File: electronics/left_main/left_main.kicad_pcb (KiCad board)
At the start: 4 copper layers, 45 x 51 mm, 189 parts, among them IC1 AS3435-EQFM, IC2 AS3435-EQFM, J1 connectors_board, J10 right_side, J11 right_side, J12 right_side, J13 right_side, J14 right_side, J15 right_side, J16 right_side, J17 right_side, J18 right_side, J19 ear_sensor, J20 ear_sensor, J21 ear_sensor, J22 ear_sensor, J3 FF_MIC_L_+, J4 FF_MIC_L_-, J5 FB_MIC_L_+, J6 FB_MIC_L_-, J7 HP_L_+, J8 HP_L_-, J9 right_side, SW2 reset_button, U1 BM83, U2 ATSAMD21G18_QFN, U3 MCP73831T-2ACI/OT, U4 SPX3819-3.3, U5 MAX17048G+T10, U6 AP2127K-1.8, U7 AP22814AW5, U8 AP22814AW5, Y1 32.768KHz

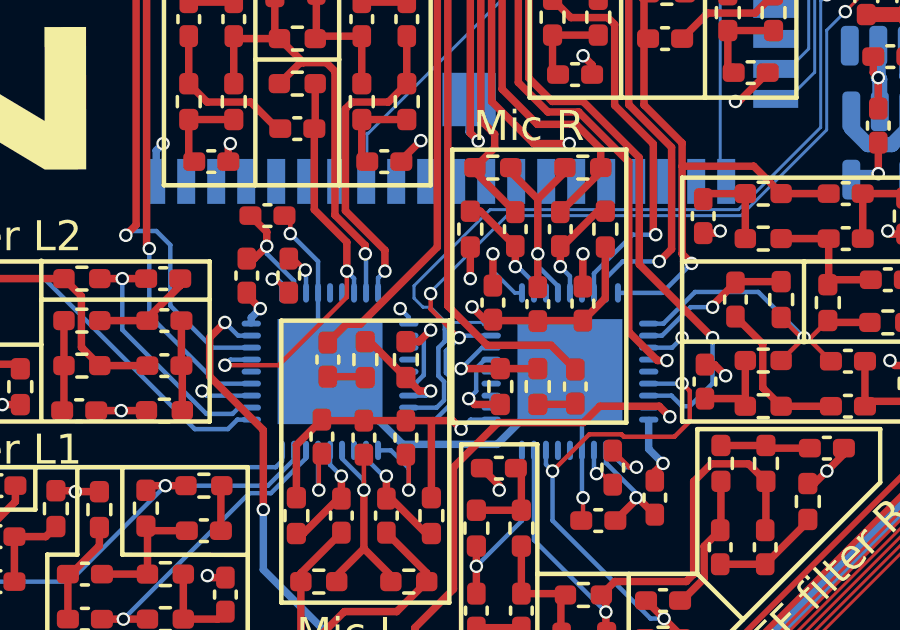
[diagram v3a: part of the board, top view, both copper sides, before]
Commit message: connectors board parts allocated
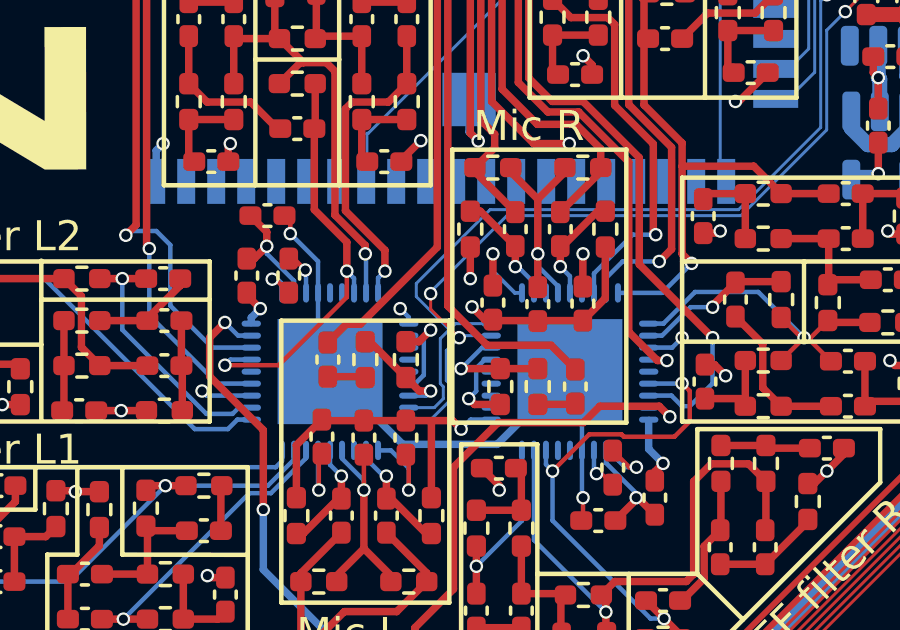
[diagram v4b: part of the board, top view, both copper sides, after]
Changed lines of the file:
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@@
   (segment (start 66.994 61.8) (end 67.296428 61.8) (width 0.15) (layer "B.Cu") (net 98))
   (segment (start 66.294 62.5) (end 66.994 61.8) (width 0.15) (layer "B.Cu") (net 98))
-  (segment (start 66.228 61.468) (end 65.278 60.518) (width 0.15) (layer "F.Cu") (net 99))
+  (segment (start 65.278 60.518) (end 66.228 61.468) (width 0.1) (layer "F.Cu") (net 99))
   (segment (start 81.2 49.5025) (end 80.6645 50.038) (width 0.1) (layer "F.Cu") (net 99))
   (segment (start 83.555188 47.498) (end 82.087342 47.498) (width 0.1) (layer "F.Cu") (net 99))
   (segment (start 80.6645 50.038) (end 79.662 50.038) (width 0.1) (layer "F.Cu") (net 99))
-  (segment (start 65.278 60.518) (end 65.278 60) (width 0.15) (layer "F.Cu") (net 99))
   (segment (start 82.087342 47.498) (end 81.2 48.385342) (width 0.1) (layer "F.Cu") (net 99))
   (segment (start 79.662 50.038) (end 79.1 50.6) (width 0.1) (layer "F.Cu") (net 99))
   (segment (start 81.2 48.385342) (end 81.2 49.5025) (width 0.1) (layer "F.Cu") (net 99))
   (segment (start 84.063188 48.006) (end 83.555188 47.498) (width 0.1) (layer "F.Cu") (net 99))
+  (segment (start 65.278 60) (end 65.278 60.518) (width 0.1) (layer "F.Cu") (net 99))
   (via (at 66.228 61.468) (size 0.45) (drill 0.3) (layers "F.Cu" "B.Cu") (net 99))
   (via (at 84.063188 48.006) (size 0.45) (drill 0.3) (layers "F.Cu" "B.Cu") (net 99))
   (via (at 65.278 60) (size 0.45) (drill 0.3) (layers "F.Cu" "B.Cu") (net 99))
   (via (at 79.1 50.6) (size 0.45) (drill 0.3) (layers "F.Cu" "B.Cu") (net 99))
-  (segment (start 65.975 63.658884) (end 65.975 62.827446) (width 0.15) (layer "B.Cu") (net 99))
-  (segment (start 66.296 61.4) (end 67.296428 61.4) (width 0.15) (layer "B.Cu") (net 99))
-  (segment (start 65.975 62.827446) (end 65.786 62.638446) (width 0.15) (layer "B.Cu") (net 99))
+  (segment (start 65.9 63.582842) (end 65.9 63) (width 0.1) (layer "B.Cu") (net 99))
+  (segment (start 65.8 61.896) (end 66.228 61.468) (width 0.1) (layer "B.Cu") (net 99))
   (segment (start 75.622842 57.4) (end 78.48 54.542842) (width 0.1) (layer "B.Cu") (net 99))
+  (segment (start 65.9 63) (end 65.8 62.9) (width 0.1) (layer "B.Cu") (net 99))
   (segment (start 67.822 57.4) (end 75.622842 57.4) (width 0.1) (layer "B.Cu") (net 99))
   (segment (start 88.876002 48.502558) (end 88.876002 48.768) (width 0.1) (layer "B.Cu") (net 99))
+  (segment (start 65.282842 64.2) (end 65.9 63.582842) (width 0.1) (layer "B.Cu") (net 99))
   (segment (start 84.571188 48.514) (end 86.564558 48.514) (width 0.1) (layer "B.Cu") (net 99))
   (segment (start 78.48 51.22) (end 79.1 50.6) (width 0.1) (layer "B.Cu") (net 99))
-  (segment (start 65.786 62.638446) (end 65.786 61.91) (width 0.15) (layer "B.Cu") (net 99))
+  (segment (start 64.55 64.2) (end 65.282842 64.2) (width 0.1) (layer "B.Cu") (net 99))
   (segment (start 83.598 47.540812) (end 83.598 46.228) (width 0.1) (layer "B.Cu") (net 99))
   (segment (start 78.48 54.542842) (end 78.48 51.22) (width 0.1) (layer "B.Cu") (net 99))
+  (segment (start 66.296 61.4) (end 67.296428 61.4) (width 0.1) (layer "B.Cu") (net 99))
   (segment (start 87.016158 48.0624) (end 88.435844 48.0624) (width 0.1) (layer "B.Cu") (net 99))
-  (segment (start 65.433885 64.2) (end 65.975 63.658884) (width 0.15) (layer "B.Cu") (net 99))
   (segment (start 84.063188 48.006) (end 84.571188 48.514) (width 0.1) (layer "B.Cu") (net 99))
-  (segment (start 64.55 64.2) (end 65.433885 64.2) (width 0.15) (layer "B.Cu") (net 99))
   (segment (start 86.564558 48.514) (end 87.016158 48.0624) (width 0.1) (layer "B.Cu") (net 99))
   (segment (start 65.278 60) (end 65.278 59.944) (width 0.1) (layer "B.Cu") (net 99))
-  (segment (start 66.228 61.468) (end 66.296 61.4) (width 0.15) (layer "B.Cu") (net 99))
-  (segment (start 65.786 61.91) (end 66.228 61.468) (width 0.15) (layer "B.Cu") (net 99))
+  (segment (start 65.8 62.9) (end 65.8 61.896) (width 0.1) (layer "B.Cu") (net 99))
+  (segment (start 66.228 61.468) (end 66.296 61.4) (width 0.1) (layer "B.Cu") (net 99))
   (segment (start 65.278 59.944) (end 67.822 57.4) (width 0.1) (layer "B.Cu") (net 99))
   (segment (start 84.063188 48.006) (end 83.598 47.540812) (width 0.1) (layer "B.Cu") (net 99))
@@
   (via (at 83.1305 46.9905) (size 0.45) (drill 0.3) (layers "F.Cu" "B.Cu") (net 100))
   (segment (start 88.376001 48.2854) (end 88.353001 48.2624) (width 0.1) (layer "B.Cu") (net 100))
-  (segment (start 65.725 61.2) (end 65.965 60.96) (width 0.1) (layer "B.Cu") (net 100))
+  (segment (start 64.8 60.1) (end 65.9 61.2) (width 0.1) (layer "B.Cu") (net 100))
+  (segment (start 65.4 63.8) (end 65.7 63.5) (width 0.1) (layer "B.Cu") (net 100))
   (segment (start 87.099 48.2624) (end 86.5934 48.768) (width 0.1) (layer "B.Cu") (net 100))
   (segment (start 86.5934 48.768) (end 83.82 48.768) (width 0.1) (layer "B.Cu") (net 100))
-  (segment (start 65.75 61.592446) (end 65.75 61.225) (width 0.15) (layer "B.Cu") (net 100))
-  (segment (start 65.725 60.899) (end 65.725 61.2) (width 0.1) (layer "B.Cu") (net 100))
-  (segment (start 64.723 59.737) (end 64.723 60.151) (width 0.1) (layer "B.Cu") (net 100))
   (segment (start 83.098 46.228) (end 83.098 46.958) (width 0.1) (layer "B.Cu") (net 100))
-  (segment (start 67.26 57.2) (end 64.723 59.737) (width 0.1) (layer "B.Cu") (net 100))
-  (segment (start 65.024 60.452) (end 65.278 60.452) (width 0.1) (layer "B.Cu") (net 100))
+  (segment (start 65.7 63.5) (end 65.7 63.1) (width 0.1) (layer "B.Cu") (net 100))
+  (segment (start 65.6 61.5) (end 65.9 61.2) (width 0.1) (layer "B.Cu") (net 100))
+  (segment (start 64.55 63.8) (end 65.4 63.8) (width 0.1) (layer "B.Cu") (net 100))
   (segment (start 78.28 54.46) (end 75.54 57.2) (width 0.1) (layer "B.Cu") (net 100))
-  (segment (start 78.28 50.244) (end 78.28 54.46) (width 0.1) (layer "B.Cu") (net 100))
-  (segment (start 64.723 60.151) (end 65.024 60.452) (width 0.1) (layer "B.Cu") (net 100))
-  (segment (start 65.536 61.806446) (end 65.75 61.592446) (width 0.15) (layer "B.Cu") (net 100))
-  (segment (start 65.278 60.452) (end 65.725 60.899) (width 0.1) (layer "B.Cu") (net 100))
-  (segment (start 65.965 60.96) (end 67.256428 60.96) (width 0.1) (layer "B.Cu") (net 100))
-  (segment (start 65.480331 63.8) (end 65.725 63.555331) (width 0.15) (layer "B.Cu") (net 100))
+  (segment (start 65.7 63.1) (end 65.6 63) (width 0.1) (layer "B.Cu") (net 100))
   (segment (start 83.1305 48.0785) (end 83.1305 46.9905) (width 0.1) (layer "B.Cu") (net 100))
-  (segment (start 65.725 62.931) (end 65.536 62.741999) (width 0.15) (layer "B.Cu") (net 100))
+  (segment (start 64.8 59.66) (end 64.8 60.1) (width 0.1) (layer "B.Cu") (net 100))
+  (segment (start 66.1 61) (end 67.296428 61) (width 0.1) (layer "B.Cu") (net 100))
+  (segment (start 65.9 61.2) (end 66.1 61) (width 0.1) (layer "B.Cu") (net 100))
+  (segment (start 88.376001 48.768) (end 88.376001 48.2854) (width 0.1) (layer "B.Cu") (net 100))
+  (segment (start 88.353001 48.2624) (end 87.099 48.2624) (width 0.1) (layer "B.Cu") (net 100))
   (segment (start 75.54 57.2) (end 67.26 57.2) (width 0.1) (layer "B.Cu") (net 100))
-  (segment (start 65.536 62.741999) (end 65.536 61.806446) (width 0.15) (layer "B.Cu") (net 100))
-  (segment (start 67.256428 60.96) (end 67.296428 61) (width 0.1) (layer "B.Cu") (net 100))
-  (segment (start 88.376001 48.768) (end 88.376001 48.2854) (width 0.1) (layer "B.Cu") (net 100))
-  (segment (start 64.55 63.8) (end 65.480331 63.8) (width 0.15) (layer "B.Cu") (net 100))
-  (segment (start 88.353001 48.2624) (end 87.099 48.2624) (width 0.1) (layer "B.Cu") (net 100))
+  (segment (start 65.6 63) (end 65.6 61.5) (width 0.1) (layer "B.Cu") (net 100))
   (segment (start 83.82 48.768) (end 83.1305 48.0785) (width 0.1) (layer "B.Cu") (net 100))
   (segment (start 78.486 50.038) (end 78.28 50.244) (width 0.1) (layer "B.Cu") (net 100))
-  (segment (start 65.725 63.555331) (end 65.725 62.931) (width 0.15) (layer "B.Cu") (net 100))
+  (segment (start 67.26 57.2) (end 64.8 59.66) (width 0.1) (layer "B.Cu") (net 100))
+  (segment (start 78.28 50.244) (end 78.28 54.46) (width 0.1) (layer "B.Cu") (net 100))
   (segment (start 83.098 46.958) (end 83.1305 46.9905) (width 0.1) (layer "B.Cu") (net 100))
   (segment (start 70.213026 53.944) (end 69.183999 53.944) (width 0.25) (layer "F.Cu") (net 102))

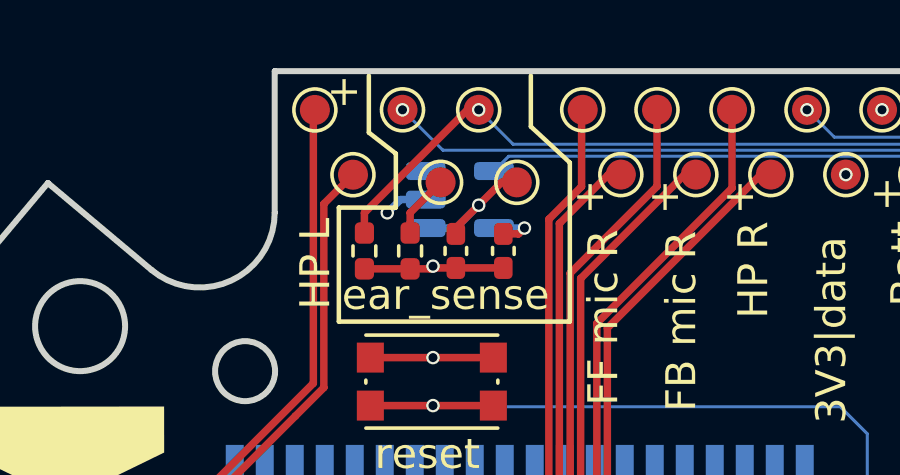
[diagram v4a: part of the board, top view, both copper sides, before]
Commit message: pcbs done, filters need to be finalised
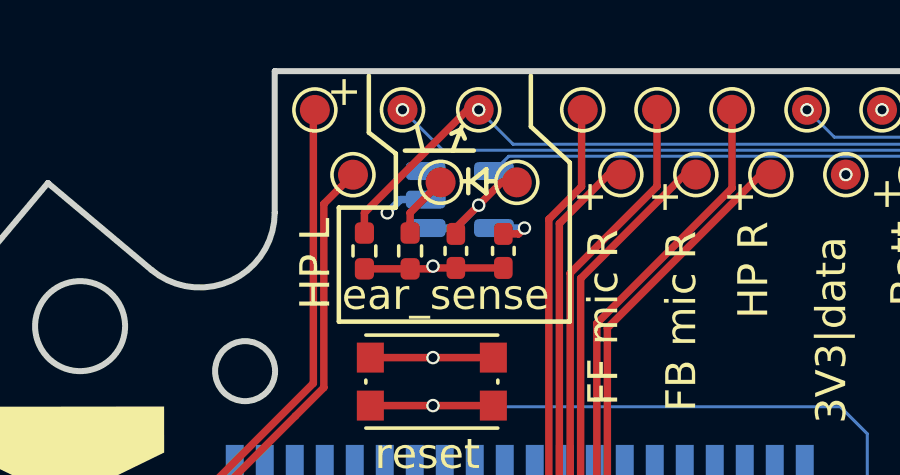
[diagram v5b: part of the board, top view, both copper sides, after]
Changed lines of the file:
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@@
       (plotinvisibletext false)
       (sketchpadsonfab false)
-      (subtractmaskfromsilk false)
+      (subtractmaskfromsilk true)
       (outputformat 1)
       (mirror false)
-      (drillshape 1)
+      (drillshape 0)
       (scaleselection 1)
-      (outputdirectory "")
+      (outputdirectory "prod/")
     )
   )
@@
     )
   )
+  (gr_line (start 63.914859 32.221874) (end 63.701007 32.223352)
+    (stroke (width 0.15) (type default)) (layer "F.SilkS"))
   (gr_line (start 77.724 58.928) (end 77.724 61.6)
     (stroke (width 0.15) (type default)) (layer "F.SilkS"))
@@
   (gr_line (start 52.5 71.6) (end 52.5 68.7)
     (stroke (width 0.15) (type default)) (layer "F.SilkS"))
+  (gr_line (start 64.514859 32.221874) (end 64.81038 32.221878)
+    (stroke (width 0.15) (type default)) (layer "F.SilkS"))
   (gr_line (start 59.436 48.006) (end 59.436 56.388)
     (stroke (width 0.15) (type default)) (layer "F.SilkS"))
+  (gr_line (start 61.8 31.2) (end 64.1 31.2)
+    (stroke (width 0.15) (type default)) (layer "F.SilkS"))
   (gr_line (start 68.834 65.024) (end 66.294 65.024)
     (stroke (width 0.15) (type default)) (layer "F.SilkS"))
@@
   (gr_rect (start 56.388 48.006) (end 65.278 56.388)
     (stroke (width 0.15) (type default)) (fill none) (layer "F.SilkS"))
+  (gr_line (start 63.659117 30.497911) (end 63.8 30.8)
+    (stroke (width 0.15) (type default)) (layer "F.SilkS"))
   (gr_line (start 59.6 33.1) (end 61.5 33.1)
     (stroke (width 0.15) (type default)) (layer "F.SilkS"))
+  (gr_line (start 64.514859 32.621874) (end 64.014859 32.221874)
+    (stroke (width 0.15) (type default)) (layer "F.SilkS"))
+  (gr_line (start 63.4 31.2) (end 63.7 30.4)
+    (stroke (width 0.15) (type default)) (layer "F.SilkS"))
   (gr_line (start 61.5 33.1) (end 61.5 31.3)
     (stroke (width 0.15) (type default)) (layer "F.SilkS"))
@@
   (gr_line (start 49.022 71.628) (end 45.212 68.326)
     (stroke (width 0.15) (type default)) (layer "F.SilkS"))
+  (gr_line (start 64.514859 31.821874) (end 64.514859 32.621874)
+    (stroke (width 0.15) (type default)) (layer "F.SilkS"))
   (gr_line (start 67.3 31.6) (end 66 30.4)
     (stroke (width 0.15) (type default)) (layer "F.SilkS"))
@@
   (gr_line (start 71.882 69.342) (end 71.882 73.406)
     (stroke (width 0.15) (type default)) (layer "F.SilkS"))
+  (gr_line (start 63.659117 30.497911) (end 63.349831 30.639448)
+    (stroke (width 0.15) (type default)) (layer "F.SilkS"))
   (gr_line (start 53.5 68.7) (end 53.5 65.8)
     (stroke (width 0.15) (type default)) (layer "F.SilkS"))
@@
   (gr_line (start 52.3 60.2) (end 57.9 60.2)
     (stroke (width 0.15) (type default)) (layer "F.SilkS"))
+  (gr_line (start 63.914859 32.621874) (end 63.914859 31.821874)
+    (stroke (width 0.15) (type default)) (layer "F.SilkS"))
   (gr_line (start 66.294 73.406) (end 73.152 73.406)
     (stroke (width 0.15) (type default)) (layer "F.SilkS"))
@@
   (gr_line (start 68.834 69.342) (end 68.834 65.024)
     (stroke (width 0.15) (type default)) (layer "F.SilkS"))
+  (gr_line (start 62.2 30.4) (end 62.4 31.2)
+    (stroke (width 0.15) (type default)) (layer "F.SilkS"))
   (gr_line (start 59.6 36.9) (end 67.3 36.9)
     (stroke (width 0.15) (type default)) (layer "F.SilkS"))
@@
   (gr_line (start 66 30.4) (end 66 28.7)
     (stroke (width 0.15) (type default)) (layer "F.SilkS"))
+  (gr_line (start 64.014859 32.221874) (end 64.514859 31.821874)
+    (stroke (width 0.15) (type default)) (layer "F.SilkS"))
   (gr_line (start 59.182 65.786) (end 59.182 71.628)
     (stroke (width 0.15) (type default)) (layer "F.SilkS"))
@@
   (gr_line (start 60.6 30.6) (end 60.6 28.7)
     (stroke (width 0.15) (type default)) (layer "F.SilkS"))
-  (gr_line (start 75 76.900783) (end 65.906666 76.900783)
+  (gr_line (start 72.25 76.900783) (end 63.156666 76.900783)
     (stroke (width 0.2) (type solid)) (layer "Dwgs.User"))
   (gr_line (start 75 86.25) (end 65.906666 86.25)

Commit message: FB,FF filter separated from main schematic
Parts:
- removed C18, C19, C26, C28, C34, C36, C42, C45, C59, C60, C63, C64: 22nF, Capacitor_SMD:C_0402_1005Metric_Pad0.74x0.62mm_HandSolder
- removed C20, C22, C24, C27, C30, C32, C35, C38, C40, C44, C51, C55, C61, C62, C67, C68, C71, C72: 33nF, Capacitor_SMD:C_0402_1005Metric_Pad0.74x0.62mm_HandSolder
- removed C21, C25, C29, C33, C37, C41, C46, C57, C65, C66, C73, C74: 4.7nF, Capacitor_SMD:C_0402_1005Metric_Pad0.74x0.62mm_HandSolder
- removed C23, C31, C39, C53, C69, C70: 15nF, Capacitor_SMD:C_0402_1005Metric_Pad0.74x0.62mm_HandSolder
- removed R12, R15, R16, R23, R25, R32, R34, R41, R54, R55, R58, R59: 3k, Resistor_SMD:R_0402_1005Metric_Pad0.72x0.64mm_HandSolder
- removed R13, R14, R24, R33, R56, R57: 5.5k, Resistor_SMD:R_0402_1005Metric_Pad0.72x0.64mm_HandSolder
- removed R17, R18, R22, R26, R27, R29, R35, R36, R38, R45, R46, R50, R60, R61, R62, R63, R66, R67: 22k, Resistor_SMD:R_0402_1005Metric_Pad0.72x0.64mm_HandSolder
- removed R19, R21, R28, R31, R37, R40, R48, R52, R64, R65, R70, R71: 6.2k, Resistor_SMD:R_0402_1005Metric_Pad0.72x0.64mm_HandSolder
- removed R20, R30, R39, R51, R68, R69: 1k, Resistor_SMD:R_0402_1005Metric_Pad0.72x0.64mm_HandSolder
- added J23: FB_Filters, Connector_Hirose:Hirose_DF12_DF12E3.0-14DP-0.5V_2x07_P0.50mm_Vertical, F.Cu at (79.9, 61.5)
- added J24: FF_Filters, Connector_Hirose:Hirose_DF12_DF12E3.0-14DP-0.5V_2x07_P0.50mm_Vertical, F.Cu at (52.5, 63.7)
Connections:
- net Net-(IC1-MIXR) renamed /HP_driver_R/FF_QOP1
- net Net-(IC2-MIXR) renamed /HP_driver_L/FF_QOP1
- IC1 pad 16: Net-(IC1-QMICR) -> /HP_driver_R/FB_QMIC
- IC1 pad 35: Net-(IC1-IOP1L) -> /HP_driver_R/FF_IOP1
- IC1 pad 36: Net-(IC1-QMICL) -> /HP_driver_R/FF_QMIC
- IC2 pad 16: Net-(IC2-QMICR) -> /HP_driver_L/FB_QMIC
- IC2 pad 35: Net-(IC2-IOP1L) -> /HP_driver_L/FF_IOP1
- IC2 pad 36: Net-(IC2-QMICL) -> /HP_driver_L/FF_QMIC
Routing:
- net /HP_driver_L/FB_QMIC: track 0.00 -> 39.0 mm, vias 0 -> 1
- net /HP_driver_L/QOP2R: track 8.80 -> 40.0 mm
- net /HP_driver_L/QOP1R: track 17.6 -> 38.7 mm
- net /HP_driver_R/FF_IOP1: track 0.00 -> 20.6 mm, vias 0 -> 1
- net /HP_driver_L/FF_QMIC: track 0.00 -> 20.5 mm, vias 0 -> 1
- net Net-(IC1-IOP1L): track 20.3 -> 0.00 mm, vias 1 -> 0
- net /HP_driver_L/FF_IOP1: track 0.00 -> 19.1 mm, vias 0 -> 1
- net /HP_driver_L/IOP1R: track 20.0 -> 39.0 mm, vias 2 -> 1
- net /HP_driver_R/FF_QMIC: track 0.00 -> 18.4 mm, vias 0 -> 1
- net /HP_driver_L/IOP2R: track 21.5 -> 39.0 mm
- net Net-(IC2-IOP1L): track 15.8 -> 0.00 mm, vias 1 -> 0
- net Net-(IC1-QMICR): track 14.9 -> 0.00 mm, vias 1 -> 0
- net /HP_driver_R/FF_QOP1: track 16.9 -> 30.5 mm
- net /HP_driver_R/IOP1R: track 20.4 -> 8.25 mm
- net /HP_driver_L/FF_QOP1: track 14.2 -> 25.1 mm
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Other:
- board text added: "FB filters"
- board text added: "FF filters"
- board text removed: "FB filter L1"
- board text removed: "FB filter L2"
- board text removed: "FB filter R1"
- board text removed: "FB filter R2"
- board text removed: "FF filter L"
- board text removed: "FF filter R"
